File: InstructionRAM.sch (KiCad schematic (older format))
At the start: 6 parts, among them U70 IDT7008L15JG, U71 ATF22V10C-7PX, U72 IDT7008L15JG

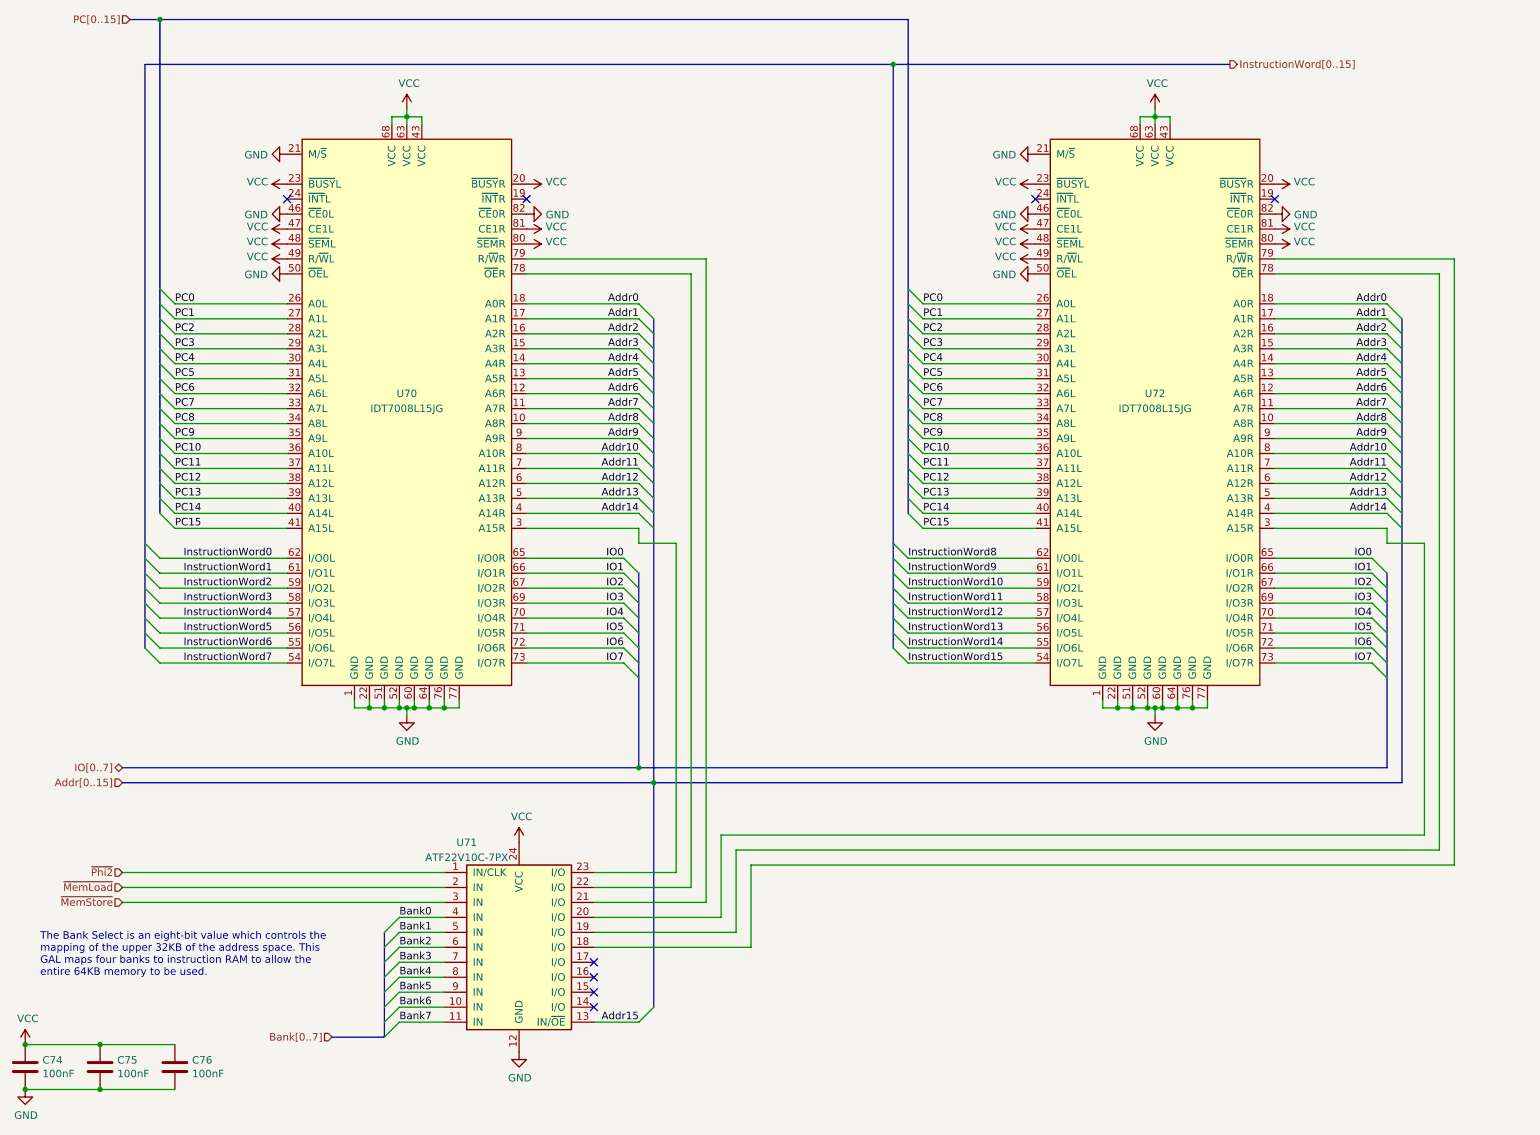
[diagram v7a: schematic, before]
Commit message: Remove Instruction RAM and replace with 45ns NOR Flash ICs.
The CPU is getting much too complicated. I can incorporate writable
instruction memory into the next version once the kinks have been worked
out.

The CPU clock speed must be reduced from 16MHz to 12MHz to accommodate
this change. Though, the rest of the CPU will be designed assuming a
62.5ns clock period (16MHz)
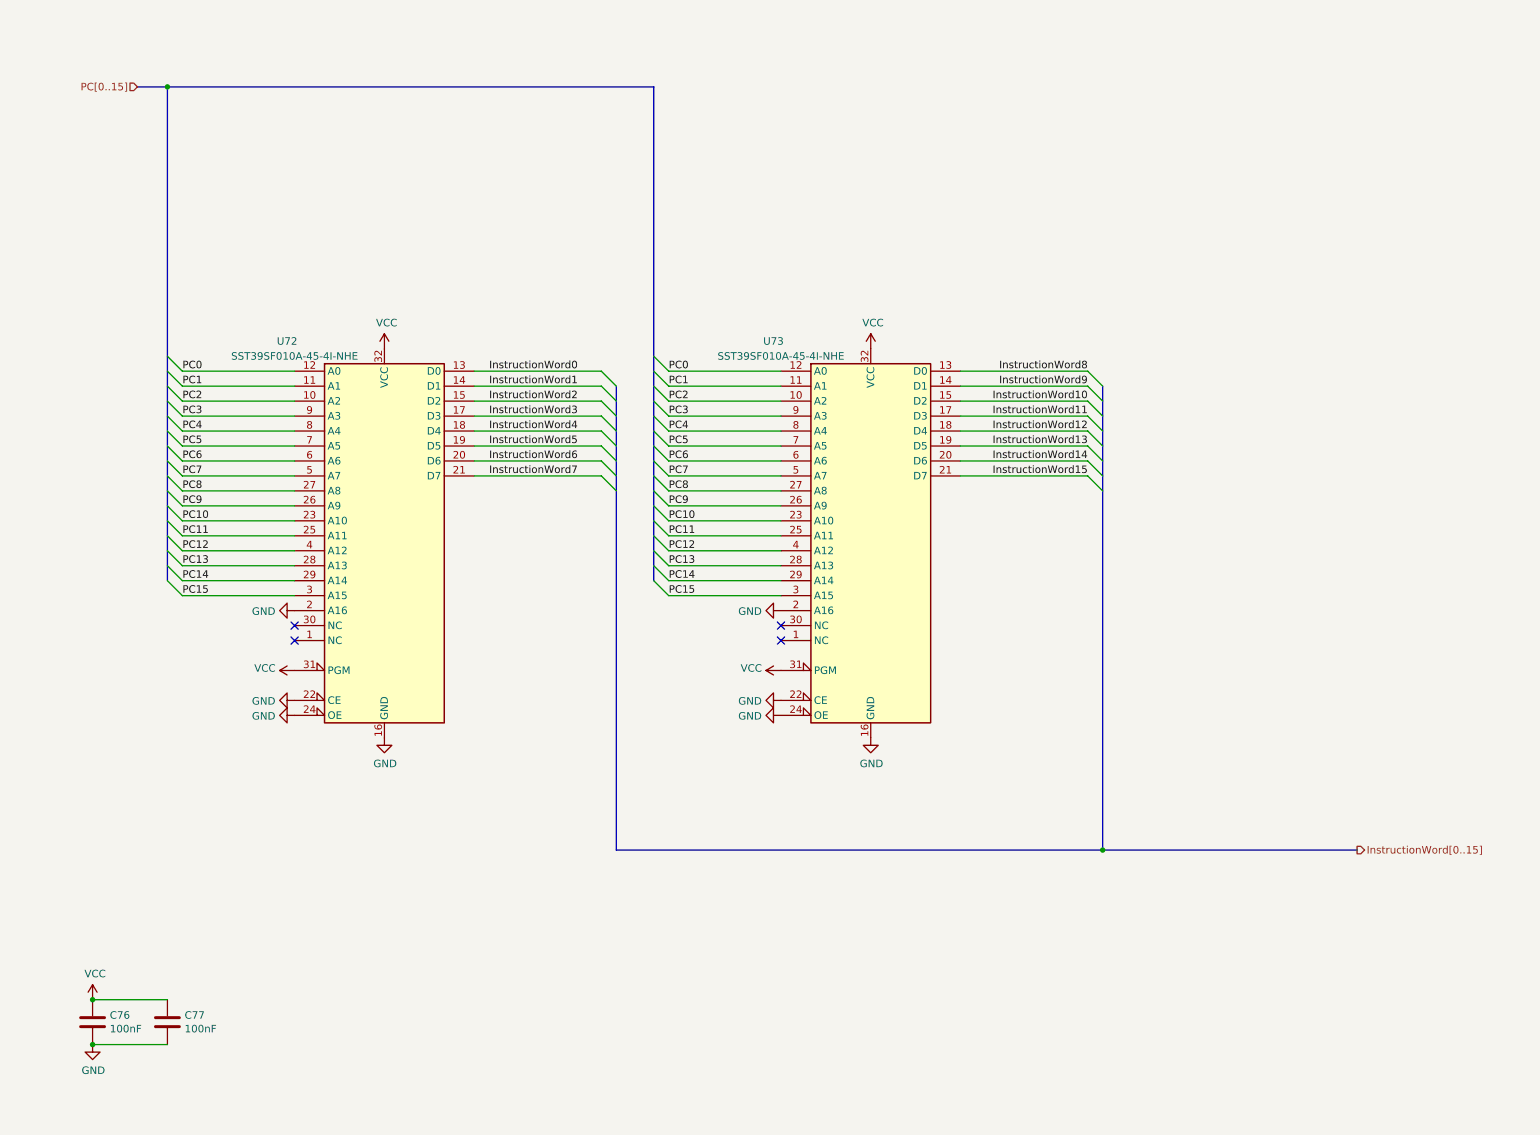
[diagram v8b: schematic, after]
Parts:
- removed C76: 100nF, Capacitor_SMD:C_0603_1608Metric_Pad1.08x0.95mm_HandSolder, symbol Device:C
- removed U70, U72: IDT7008L15JG, Package_LCC:PLCC-84_SMD-Socket, symbol Memory_RAM:IDT7008L15JG
- removed U71: ATF22V10C-7PX, Package_DIP:DIP-24_W8.89mm_SMDSocket_LongPads, symbol MainBoard-rescue:ATF22V10C-Logic_Programmable
- added U72, U73: SST39SF010A-45-4I-NHE, Socket:DIP_Socket-32_W11.9_W12.7_W15.24_W17.78_W18.5_3M_232-1285-00-0602J, symbol Memory_Flash:SST39SF010
- renumbered C74 to C76, C75 to C77
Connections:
- net GND: now also U72.16 (GND), U72.2 (A16), U72.22 (CE), U72.24 (OE), U73.16 (GND), U73.2 (A16), U73.22 (CE), U73.24 (OE)
- net InstructionWord0: now also U72.13 (D0)
- net InstructionWord1: now also U72.14 (D1)
- net InstructionWord10: now also U73.15 (D2)
- net InstructionWord11: now also U73.17 (D3)
- net InstructionWord12: now also U73.18 (D4)
- net InstructionWord13: now also U73.19 (D5)
- net InstructionWord14: now also U73.20 (D6)
- net InstructionWord15: now also U73.21 (D7)
- net InstructionWord2: now also U72.15 (D2)
- net InstructionWord3: now also U72.17 (D3)
- net InstructionWord4: now also U72.18 (D4)
- net InstructionWord5: now also U72.19 (D5)
- net InstructionWord6: now also U72.20 (D6)
- net InstructionWord7: now also U72.21 (D7)
- net InstructionWord8: now also U73.13 (D0)
- net InstructionWord9: now also U73.14 (D1)
- net PC0: now also U72.12 (A0), U73.12 (A0)
- net PC1: now also U72.11 (A1), U73.11 (A1)
- net PC10: now also U72.23 (A10), U73.23 (A10)
- net PC11: now also U72.25 (A11), U73.25 (A11)
- net PC12: now also U72.4 (A12), U73.4 (A12)
- net PC13: now also U72.28 (A13), U73.28 (A13)
- net PC14: now also U72.29 (A14), U73.29 (A14)
- net PC15: now also U72.3 (A15), U73.3 (A15)
- net PC2: now also U72.10 (A2), U73.10 (A2)
- net PC3: now also U72.9 (A3), U73.9 (A3)
- net PC4: now also U72.8 (A4), U73.8 (A4)
- net PC5: now also U72.7 (A5), U73.7 (A5)
- net PC6: now also U72.6 (A6), U73.6 (A6)
- net PC7: now also U72.5 (A7), U73.5 (A7)
- net PC8: now also U72.27 (A8), U73.27 (A8)
- net PC9: now also U72.26 (A9), U73.26 (A9)
- net VCC: now also U72.31 (PGM), U72.32 (VCC), U73.31 (PGM), U73.32 (VCC)
- no-connect marks 8 -> 4
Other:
- note removed: "The Bank Select is an eight-bit value which controls the\nmapping of the upper 32KB of the address space. This\nGAL maps four banks to instruction RAM to allow the\nentire 64KB memory to be used."
- moved on the sheet: C76, C77
